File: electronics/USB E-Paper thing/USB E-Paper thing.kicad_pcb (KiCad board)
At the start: 2 copper layers, 79 x 36.7 mm, 98 parts, among them J3 EXTRA2, J5 SWD, J6 USB 2.0 right angle, J8 POWER_MEASUREMENT, Q1 AO3400A, Q2 AO3401A, Q3 AO3400A, SW1 BUTTON0, SW2 BUTTON1, SW3 BUTTON2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

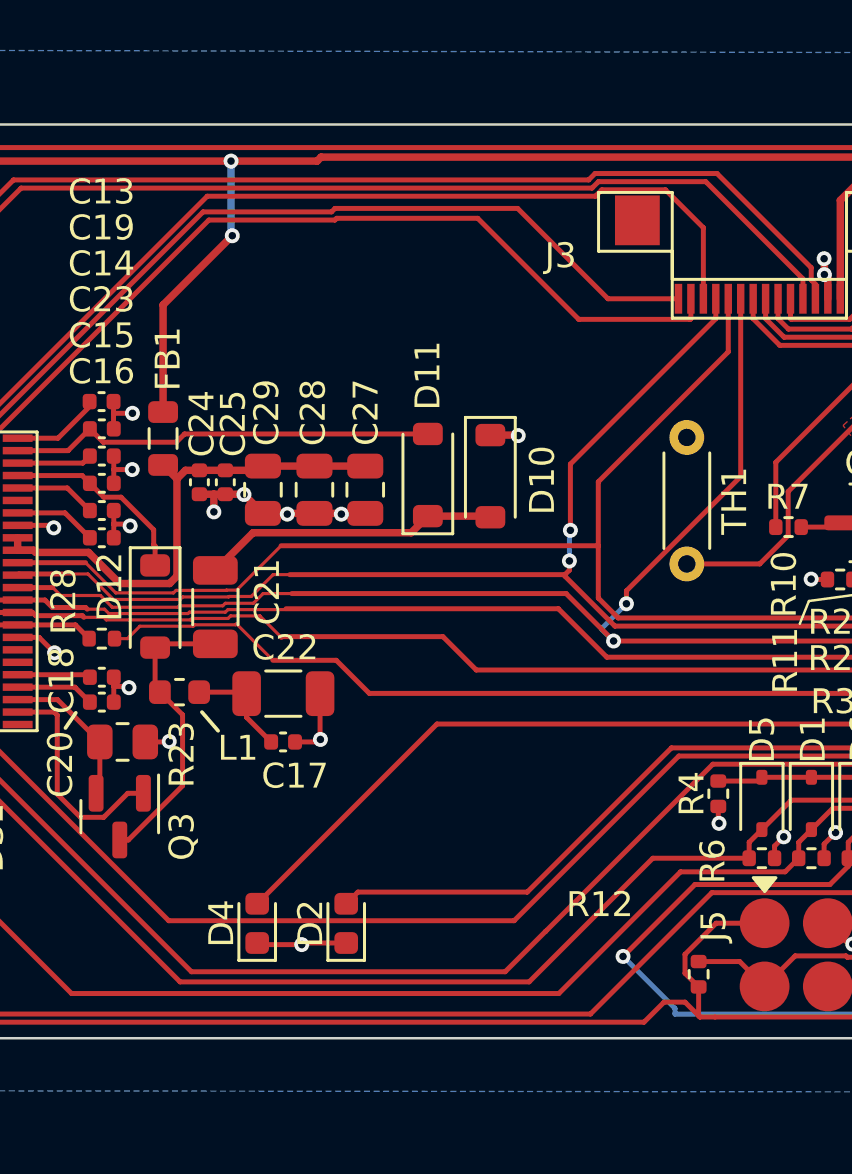
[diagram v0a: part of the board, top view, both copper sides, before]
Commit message: add adapter board
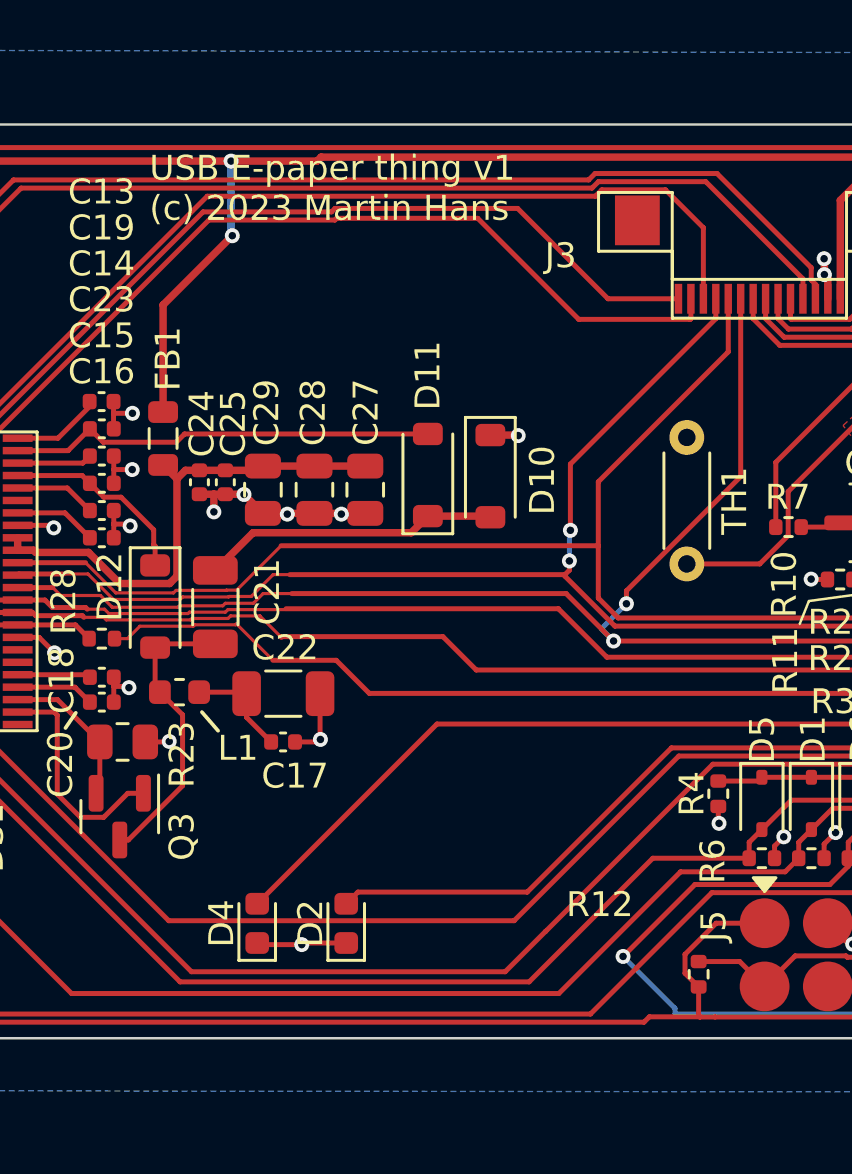
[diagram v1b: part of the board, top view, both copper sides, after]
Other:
- board text added: "USB E-paper thing v1 (c) 2023 Martin Hans"
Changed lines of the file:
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@@
   (gr_line (start 152.935 115.175) (end 149.265 111.505)
     (stroke (width 0.1) (type default)) (layer "User.1"))
+  (gr_text "USB E-paper thing v1\n(c) 2023 Martin Hans" (at 114.99 103.95) (layer "F.SilkS")
+    (effects (font (size 1 1) (thickness 0.15)) (justify left bottom))
+  )
   (dimension (type aligned) (layer "F.SilkS")
     (pts (xy 100 100) (xy 100 136.7))
@@
   (segment (start 176.1 110.75) (end 176.1 107.15) (width 0.5) (layer "F.Cu") (net 6))
   (segment (start 165.894 103.604) (end 163.694 101.404) (width 0.5) (layer "F.Cu") (net 6))
-  (segment (start 105.055 136.055) (end 134.856261 136.055) (width 0.2) (layer "F.Cu") (net 6))
   (segment (start 157.560589 112.520323) (end 156.508788 113.572124) (width 0.2) (layer "F.Cu") (net 6))
   (segment (start 137.71 135.847) (end 151.173 135.847) (width 0.2) (layer "F.Cu") (net 6))
@@
   (segment (start 152.4 117.117766) (end 152.4 118.05) (width 0.3) (layer "F.Cu") (net 6))
   (segment (start 176.171 111.241) (end 175.89 110.96) (width 0.3) (layer "F.Cu") (net 6))
-  (segment (start 102.8 133.8) (end 105.055 136.055) (width 0.2) (layer "F.Cu") (net 6))
   (segment (start 175.123 133.169576) (end 176.1 132.192576) (width 0.5) (layer "F.Cu") (net 6))
-  (segment (start 136.5035 135.2505) (end 137.1 135.847) (width 0.2) (layer "F.Cu") (net 6))
   (segment (start 154.511212 113.572124) (end 155.55 113.572124) (width 0.3) (layer "F.Cu") (net 6))
   (segment (start 161.67 120.49) (end 161.429088 120.49) (width 0.2) (layer "F.Cu") (net 6))
@@
   (segment (start 161.429088 120.49) (end 160.397876 119.458788) (width 0.3) (layer "F.Cu") (net 6))
   (segment (start 158.81 135.95) (end 166.61827 135.95) (width 0.5) (layer "F.Cu") (net 6))
+  (segment (start 135.071261 135.84) (end 137.093 135.84) (width 0.2) (layer "F.Cu") (net 6))
   (segment (start 154.252888 124.245934) (end 154.700002 124.245934) (width 0.5) (layer "F.Cu") (net 6))
   (segment (start 151.682785 116.400551) (end 151.508835 116.400551) (width 0.2) (layer "F.Cu") (net 6))
@@
   (segment (start 146.072 101.31) (end 146.166 101.404) (width 0.3) (layer "F.Cu") (net 6))
   (segment (start 151.508835 116.400551) (end 150.868284 115.76) (width 0.2) (layer "F.Cu") (net 6))
+  (segment (start 102.8 133.8) (end 105.055 136.055) (width 0.2) (layer "F.Cu") (net 6))
   (segment (start 155.72 128.79) (end 155.72 128.04) (width 0.5) (layer "F.Cu") (net 6))
+  (segment (start 134.856261 136.055) (end 135.071261 135.84) (width 0.2) (layer "F.Cu") (net 6))
   (segment (start 118.27 101.47) (end 105.94 101.47) (width 0.3) (layer "F.Cu") (net 6))
   (segment (start 115.54 111.55) (end 115.54 107.248) (width 0.3) (layer "F.Cu") (net 6))
   (segment (start 172.44 135.9) (end 173.67 135.9) (width 0.5) (layer "F.Cu") (net 6))
   (segment (start 154.252888 124.245934) (end 154.252888 123.644382) (width 0.5) (layer "F.Cu") (net 6))
-  (segment (start 134.856261 136.055) (end 135.660761 135.2505) (width 0.2) (layer "F.Cu") (net 6))
   (segment (start 176.171 123.85) (end 176.171 111.241) (width 0.3) (layer "F.Cu") (net 6))
+  (segment (start 105.055 136.055) (end 134.856261 136.055) (width 0.2) (layer "F.Cu") (net 6))
   (segment (start 155.06 120.71) (end 155.06 122.799088) (width 0.2) (layer "F.Cu") (net 6))
   (segment (start 150.868284 115.76) (end 149.87 115.76) (width 0.2) (layer "F.Cu") (net 6))
@@
   (segment (start 153.83 119.48) (end 155.06 120.71) (width 0.3) (layer "F.Cu") (net 6))
   (segment (start 165.953 104.135972) (end 165.894 104.076972) (width 0.5) (layer "F.Cu") (net 6))
+  (segment (start 137.093 135.84) (end 137.1 135.847) (width 0.2) (layer "F.Cu") (net 6))
   (segment (start 176.171 129.479) (end 176.171 123.85) (width 0.5) (layer "F.Cu") (net 6))
   (segment (start 102.9 102.95) (end 103.98 101.87) (width 0.2) (layer "F.Cu") (net 6))
@@
   (segment (start 139.7 132.08) (end 137.754312 132.08) (width 0.2) (layer "F.Cu") (net 6))
   (segment (start 144.27 101.31) (end 146.072 101.31) (width 0.3) (layer "F.Cu") (net 6))
-  (segment (start 135.660761 135.2505) (end 136.5035 135.2505) (width 0.2) (layer "F.Cu") (net 6))
   (segment (start 137.1 135.847) (end 137.71 135.847) (width 0.2) (layer "F.Cu") (net 6))
   (segment (start 155.119397 115.807) (end 153.83 117.096397) (width 0.3) (layer "F.Cu") (net 6))

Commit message: fix TP4056 footprint
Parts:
- U3: footprint Package_SO:SOP-8-1EP_4.57x4.57mm_P1.27mm_EP4.57x4.45mm -> local:ESOP-8_L4.9-W3.9-P1.27-LS6.0-BL-EP
- moved J3 2.40 mm to (139.5, 104.6)
- moved DS1 2.30 mm to (107.4, 118.3)
- turned BT1 to 0 degrees
- turned U3 to 180 degrees
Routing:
- net GND: track 120.2 -> 134.2 mm, vias 82 -> 92
- net /VBUS: track 54.0 -> 55.7 mm
- net Net-(U3-PROG): track 2.53 -> 3.77 mm
- net Net-(U3-~{STDBY}): track 4.19 -> 5.43 mm
- net Net-(U3-~{CHRG}): track 9.91 -> 11.2 mm
- net +BATT: track 93.3 -> 94.4 mm
